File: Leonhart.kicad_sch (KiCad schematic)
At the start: 0 parts

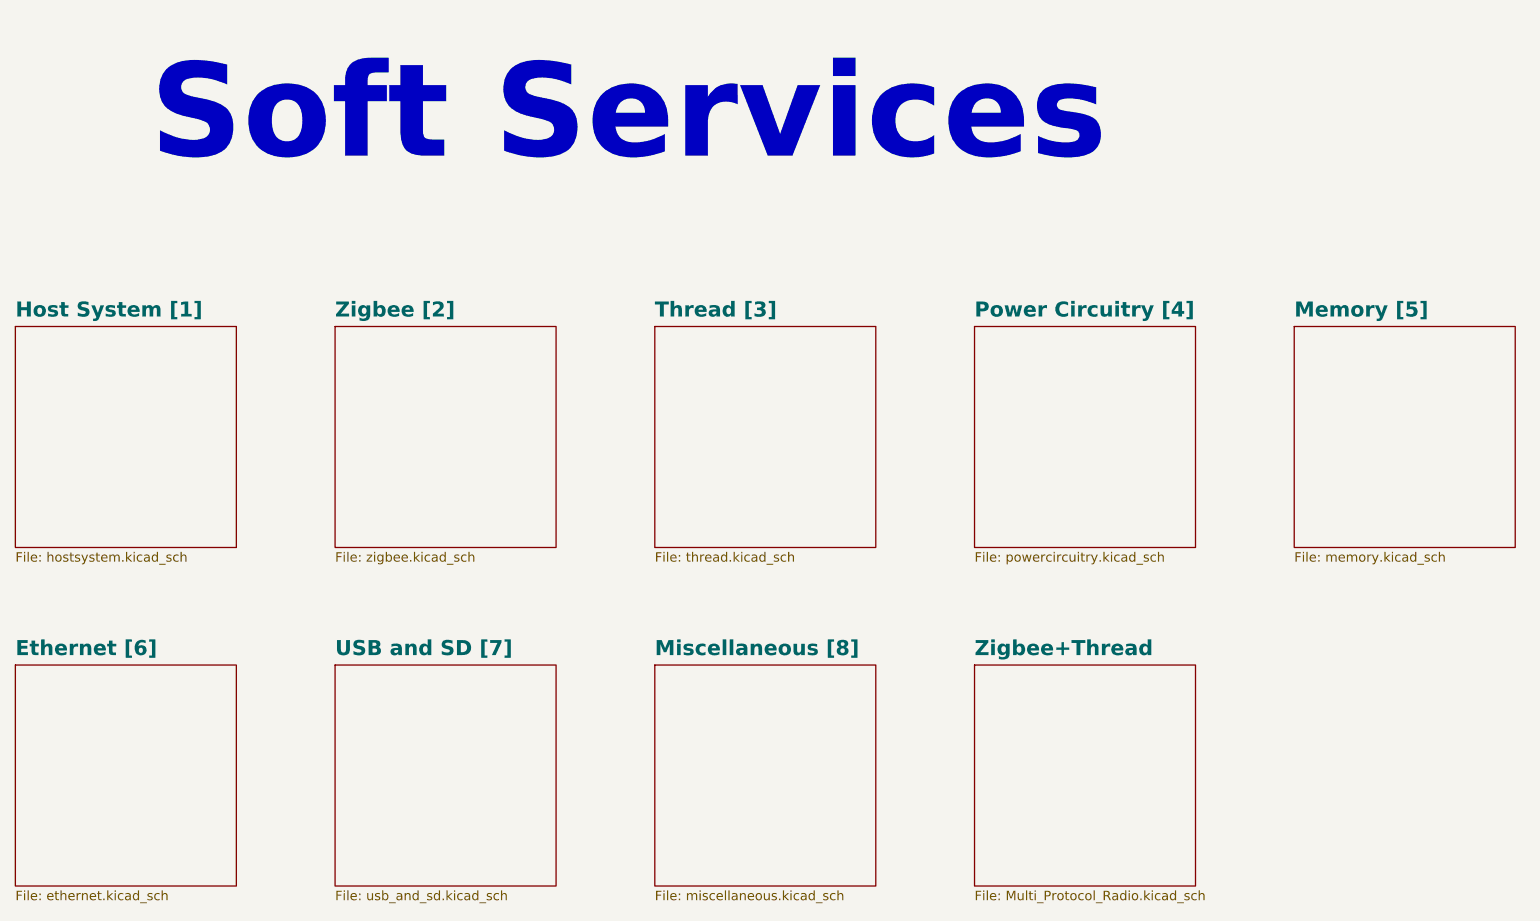
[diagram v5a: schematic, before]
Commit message: Added new radio schematic
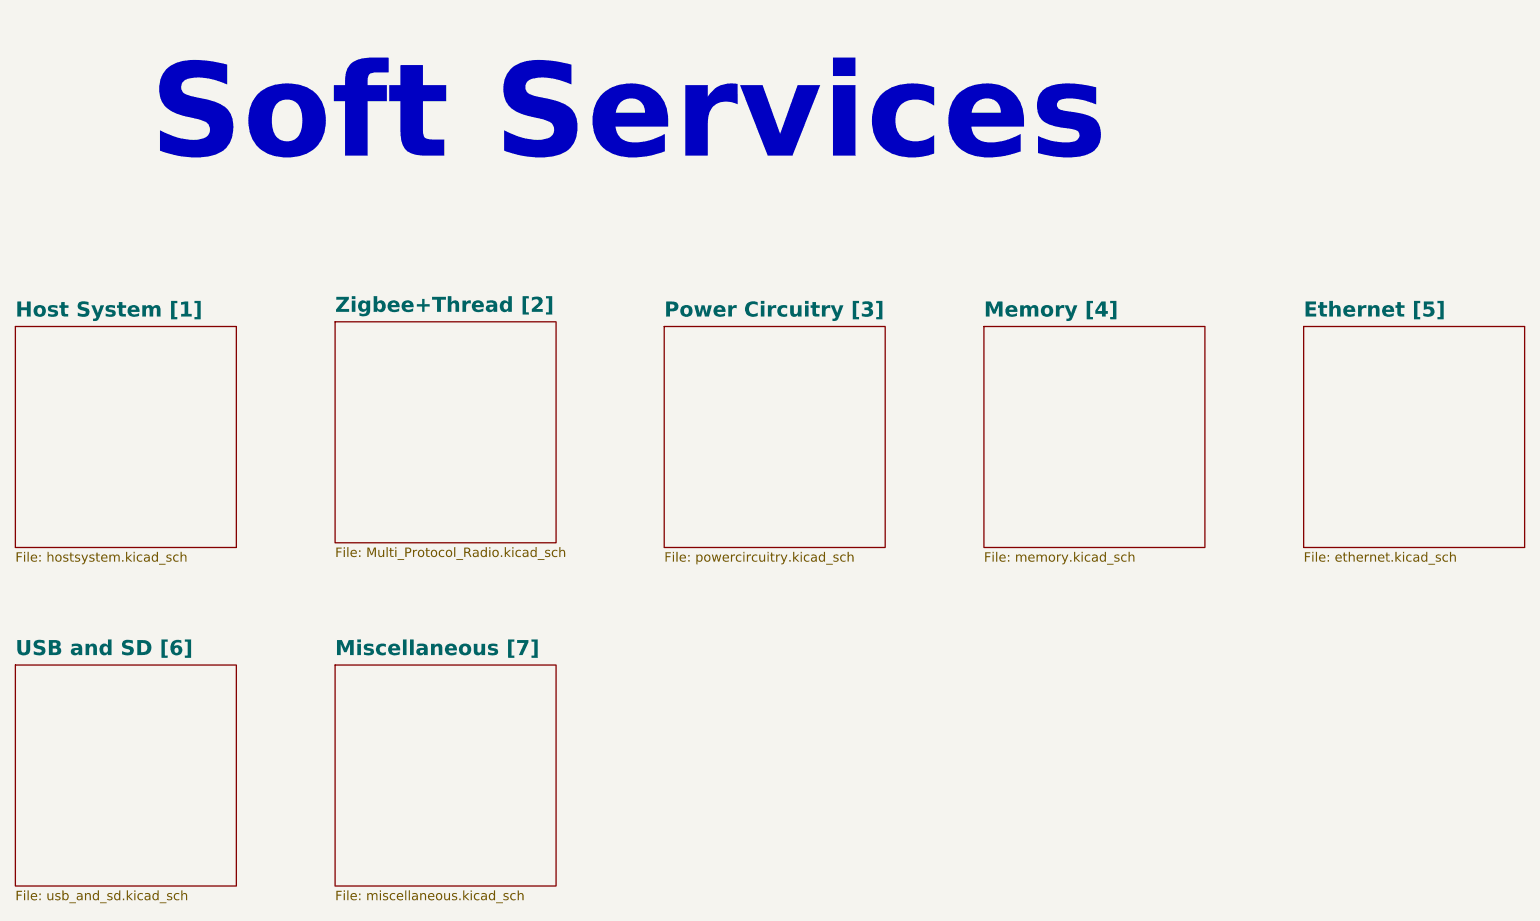
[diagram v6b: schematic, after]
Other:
- sheet Ethernet [6] renamed Ethernet [5]
- sheet Memory [5] renamed Memory [4]
- sheet Miscellaneous [8] renamed Miscellaneous [7]
- sheet Power Circuitry [4] renamed Power Circuitry [3]
- sheet USB and SD [7] renamed USB and SD [6]
- sheet Zigbee+Thread renamed Zigbee+Thread [2]
- removed sheet Thread [3]
- removed sheet Zigbee [2]
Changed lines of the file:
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@@
 	)
 	(sheet
-		(at 210.82 63.5)
-		(size 29.845 29.845)
-		(exclude_from_sim no)
-		(in_bom yes)
-		(on_board yes)
-		(dnp no)
-		(fields_autoplaced yes)
-		(stroke
-			(width 0.1524)
-			(type solid)
-		)
-		(fill
-			(color 0 0 0 0.0000)
-		)
-		(property "Sheetname" "Memory [5]"
-			(at 210.82 62.4074 0)
+		(at 168.91 63.5)
+		(size 29.845 29.845)
+		(exclude_from_sim no)
+		(in_bom yes)
+		(on_board yes)
+		(dnp no)
+		(fields_autoplaced yes)
+		(stroke
+			(width 0.1524)
+			(type solid)
+		)
+		(fill
+			(color 0 0 0 0.0000)
+		)
+		(property "Sheetname" "Memory [4]"
+			(at 168.91 62.4074 0)
 			(effects
 				(font
@@
 		)
 		(property "Sheetfile" "memory.kicad_sch"
-			(at 210.82 93.9296 0)
-			(effects
-				(font
-					(size 1.27 1.27)
-				)
-				(justify left top)
-			)
-		)
-		(instances
-			(project "Leonhart"
-				(path "/b43b7bca-e50d-42ec-8ff0-e0016dfefe0a"
-					(page "4")
-				)
-			)
-		)
-	)
-	(sheet
-		(at 167.64 63.5)
-		(size 29.845 29.845)
-		(exclude_from_sim no)
-		(in_bom yes)
-		(on_board yes)
-		(dnp no)
-		(fields_autoplaced yes)
-		(stroke
-			(width 0.1524)
-			(type solid)
-		)
-		(fill
-			(color 0 0 0 0.0000)
-		)
-		(property "Sheetname" "Power Circuitry [4]"
-			(at 167.64 62.4074 0)
+			(at 168.91 93.9296 0)
+			(effects
+				(font
+					(size 1.27 1.27)
+				)
+				(justify left top)
+			)
+		)
+		(instances
+			(project "Leonhart"
+				(path "/b43b7bca-e50d-42ec-8ff0-e0016dfefe0a"
+					(page "3")
+				)
+			)
+		)
+	)
+	(sheet
+		(at 125.73 63.5)
+		(size 29.845 29.845)
+		(exclude_from_sim no)
+		(in_bom yes)
+		(on_board yes)
+		(dnp no)
+		(fields_autoplaced yes)
+		(stroke
+			(width 0.1524)
+			(type solid)
+		)
+		(fill
+			(color 0 0 0 0.0000)
+		)
+		(property "Sheetname" "Power Circuitry [3]"
+			(at 125.73 62.4074 0)
 			(effects
 				(font
@@
 		)
 		(property "Sheetfile" "powercircuitry.kicad_sch"
-			(at 167.64 93.9296 0)
-			(effects
-				(font
-					(size 1.27 1.27)
-				)
-				(justify left top)
-			)
-		)
-		(instances
-			(project "Leonhart"
-				(path "/b43b7bca-e50d-42ec-8ff0-e0016dfefe0a"
-					(page "3")
-				)
-			)
-		)
-	)
-	(sheet
-		(at 81.28 63.5)
-		(size 29.845 29.845)
-		(exclude_from_sim no)
-		(in_bom yes)
-		(on_board yes)
-		(dnp no)
-		(fields_autoplaced yes)
-		(stroke
-			(width 0.1524)
-			(type solid)
-		)
-		(fill
-			(color 0 0 0 0.0000)
-		)
-		(property "Sheetname" "Zigbee [2]"
-			(at 81.28 62.4074 0)
-			(effects
-				(font
-					(size 2.032 2.032)
-					(thickness 0.4064)
-					(bold yes)
-				)
-				(justify left bottom)
-			)
-		)
-		(property "Sheetfile" "zigbee.kicad_sch"
-			(at 81.28 93.9296 0)
-			(effects
-				(font
-					(size 1.27 1.27)
-				)
-				(justify left top)
-			)
-		)
-		(instances
-			(project "Leonhart"
-				(path "/b43b7bca-e50d-42ec-8ff0-e0016dfefe0a"
-					(page "1")
+			(at 125.73 93.9296 0)
+			(effects
+				(font
+					(size 1.27 1.27)
+				)
+				(justify left top)
+			)
+		)
+		(instances
+			(project "Leonhart"
+				(path "/b43b7bca-e50d-42ec-8ff0-e0016dfefe0a"
+					(page "2")
 				)
 			)
@@
 	)
 	(sheet
-		(at 124.46 109.22)
-		(size 29.845 29.845)
-		(exclude_from_sim no)
-		(in_bom yes)
-		(on_board yes)
-		(dnp no)
-		(fields_autoplaced yes)
-		(stroke
-			(width 0.1524)
-			(type solid)
-		)
-		(fill
-			(color 0 0 0 0.0000)
-		)
-		(property "Sheetname" "Miscellaneous [8]"
-			(at 124.46 108.1274 0)
+		(at 81.28 109.22)
+		(size 29.845 29.845)
+		(exclude_from_sim no)
+		(in_bom yes)
+		(on_board yes)
+		(dnp no)
+		(fields_autoplaced yes)
+		(stroke
+			(width 0.1524)
+			(type solid)
+		)
+		(fill
+			(color 0 0 0 0.0000)
+		)
+		(property "Sheetname" "Miscellaneous [7]"
+			(at 81.28 108.1274 0)
 			(effects
 				(font
@@
 		)
 		(property "Sheetfile" "miscellaneous.kicad_sch"
-			(at 124.46 139.6496 0)
-			(effects
-				(font
-					(size 1.27 1.27)
-				)
-				(justify left top)
-			)
-		)
-		(instances
-			(project "Leonhart"
-				(path "/b43b7bca-e50d-42ec-8ff0-e0016dfefe0a"
-					(page "7")
+			(at 81.28 139.6496 0)
+			(effects
+				(font
+					(size 1.27 1.27)
+				)
+				(justify left top)
+			)
+		)
+		(instances
+			(project "Leonhart"
+				(path "/b43b7bca-e50d-42ec-8ff0-e0016dfefe0a"
+					(page "6")
+				)
+			)
+		)
+	)
+	(sheet
+		(at 212.09 63.5)
+		(size 29.845 29.845)
+		(exclude_from_sim no)
+		(in_bom yes)
+		(on_board yes)
+		(dnp no)
+		(fields_autoplaced yes)
+		(stroke
+			(width 0.1524)
+			(type solid)
+		)
+		(fill
+			(color 0 0 0 0.0000)
+		)
+		(property "Sheetname" "Ethernet [5]"
+			(at 212.09 62.4074 0)
+			(effects
+				(font
+					(size 2.032 2.032)
+					(thickness 0.4064)
+					(bold yes)
+				)
+				(justify left bottom)
+			)
+		)
+		(property "Sheetfile" "ethernet.kicad_sch"
+			(at 212.09 93.9296 0)
+			(effects
+				(font
+					(size 1.27 1.27)
+				)
+				(justify left top)
+			)
+		)
+		(instances
+			(project "Leonhart"
+				(path "/b43b7bca-e50d-42ec-8ff0-e0016dfefe0a"
+					(page "4")
+				)
+			)
+		)
+	)
+	(sheet
+		(at 81.28 62.865)
+		(size 29.845 29.845)
+		(exclude_from_sim no)
+		(in_bom yes)
+		(on_board yes)
+		(dnp no)
+		(fields_autoplaced yes)
+		(stroke
+			(width 0.1524)
+			(type solid)
+		)
+		(fill
+			(color 0 0 0 0.0000)
+		)
+		(property "Sheetname" "Zigbee+Thread [2]"
+			(at 81.28 61.7724 0)
+			(effects
+				(font
+					(size 2.032 2.032)
+					(thickness 0.4064)
+					(bold yes)
+				)
+				(justify left bottom)
+			)
+		)
+		(property "Sheetfile" "Multi_Protocol_Radio.kicad_sch"
+			(at 81.28 93.2946 0)
+			(effects
+				(font
+					(size 1.27 1.27)
+				)
+				(justify left top)
+			)
+		)
+		(instances
+			(project "Leonhart"
+				(path "/b43b7bca-e50d-42ec-8ff0-e0016dfefe0a"
+					(page "1")
 				)
 			)
@@
 			(color 0 0 0 0.0000)
 		)
-		(property "Sheetname" "Ethernet [6]"
+		(property "Sheetname" "USB and SD [6]"
 			(at 38.1 108.1274 0)
 			(effects
@@
 			)
 		)
-		(property "Sheetfile" "ethernet.kicad_sch"
+		(property "Sheetfile" "usb_and_sd.kicad_sch"
 			(at 38.1 139.6496 0)
 			(effects
@@
 				)
 			)
-		)
-	)
-	(sheet
-		(at 167.64 109.22)
-		(size 29.845 29.845)
-		(exclude_from_sim no)
-		(in_bom yes)
-		(on_board yes)
-		(dnp no)
-		(fields_autoplaced yes)
-		(stroke
-			(width 0.1524)
-			(type solid)
-		)
-		(fill
-			(color 0 0 0 0.0000)
-		)
-		(property "Sheetname" "Zigbee+Thread"
-			(at 167.64 108.1274 0)
-			(effects
-				(font
-					(size 2.032 2.032)
-					(thickness 0.4064)
-					(bold yes)
-				)
-				(justify left bottom)
-			)
-		)
-		(property "Sheetfile" "Multi_Protocol_Radio.kicad_sch"
-			(at 167.64 139.6496 0)
-			(effects
-				(font
-					(size 1.27 1.27)
-				)
-				(justify left top)
-			)
-		)
-		(instances
-			(project "Leonhart"
-				(path "/b43b7bca-e50d-42ec-8ff0-e0016dfefe0a"
-					(page "9")
-				)
-			)
-		)
-	)
-	(sheet
-		(at 124.46 63.5)
-		(size 29.845 29.845)
-		(exclude_from_sim no)
-		(in_bom yes)
-		(on_board yes)
-		(dnp no)
-		(fields_autoplaced yes)
-		(stroke
-			(width 0.1524)
-			(type solid)
-		)
-		(fill
-			(color 0 0 0 0.0000)
-		)
-		(property "Sheetname" "Thread [3]"
-			(at 124.46 62.4074 0)
-			(effects
-				(font
-					(size 2.032 2.032)
-					(thickness 0.4064)
-					(bold yes)
-				)
-				(justify left bottom)
-			)
-		)
-		(property "Sheetfile" "thread.kicad_sch"
-			(at 124.46 93.9296 0)
-			(effects
-				(font
-					(size 1.27 1.27)
-				)
-				(justify left top)
-			)
-		)
-		(instances
-			(project "Leonhart"
-				(path "/b43b7bca-e50d-42ec-8ff0-e0016dfefe0a"
-					(page "2")
-				)
-			)
-		)
-	)
-	(sheet
-		(at 81.28 109.22)
-		(size 29.845 29.845)
-		(exclude_from_sim no)
-		(in_bom yes)
-		(on_board yes)
-		(dnp no)
-		(fields_autoplaced yes)
-		(stroke
-			(width 0.1524)
-			(type solid)
-		)
-		(fill
-			(color 0 0 0 0.0000)
-		)
-		(property "Sheetname" "USB and SD [7]"
-			(at 81.28 108.1274 0)
-			(effects
-				(font
-					(size 2.032 2.032)
-					(thickness 0.4064)
-					(bold yes)
-				)
-				(justify left bottom)
-			)
-		)
-		(property "Sheetfile" "usb_and_sd.kicad_sch"
-			(at 81.28 139.6496 0)
-			(effects
-				(font
-					(size 1.27 1.27)
-				)
-				(justify left top)
-			)
-		)
-		(instances
-			(project "Leonhart"
-				(path "/b43b7bca-e50d-42ec-8ff0-e0016dfefe0a"
-					(page "6")
-				)
-			)

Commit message: Routed JTAG and UART header pins for SoC
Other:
- note added: "Leonhart"
- note removed: "Soft Services"
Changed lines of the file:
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@@
 	(generator_version "9.0")
 	(paper "A4")
-	(text "Soft Services"
+	(text "Leonhart"
 		(exclude_from_sim no)
 		(at 120.904 34.798 0)

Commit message: Small schematic naming change and added silkscreen to buttons and header pins
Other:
- sheet USB and SD [6] renamed USB and MMC [6]
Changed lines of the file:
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@@
 			(color 0 0 0 0.0000)
 		)
-		(property "Sheetname" "USB and SD [6]"
+		(property "Sheetname" "USB and MMC [6]"
 			(at 38.1 108.1274 0)
 			(effects
